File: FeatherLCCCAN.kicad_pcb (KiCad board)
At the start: 2 copper layers, 96.5 x 22.9 mm, 6 parts, among them J301 RJ45, J302 RJ45, U301 TCAN332DR

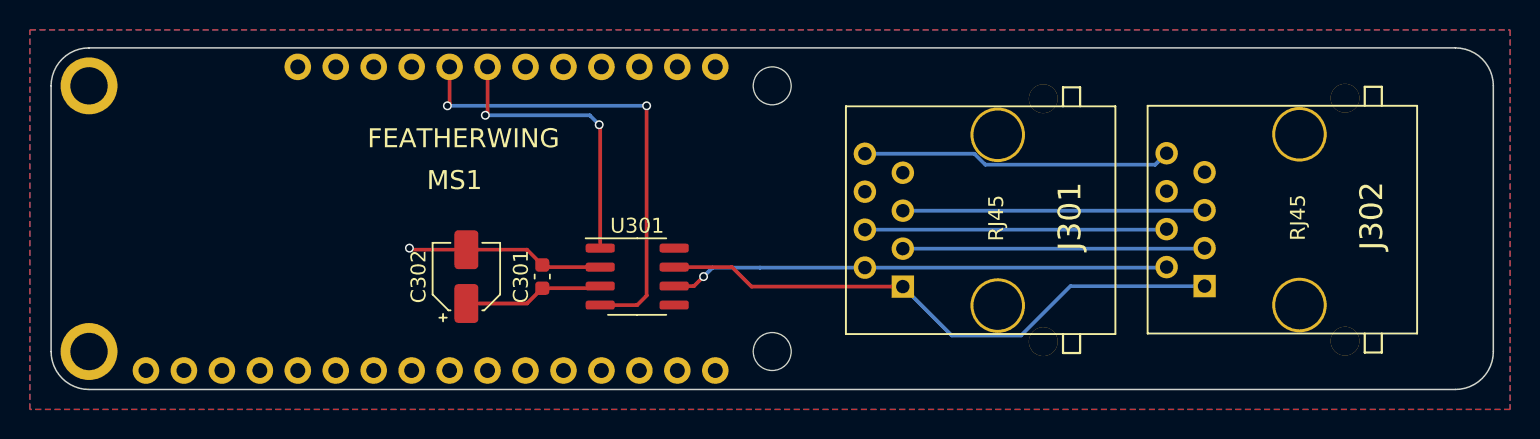
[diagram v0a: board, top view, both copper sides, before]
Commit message: Update part numbers.
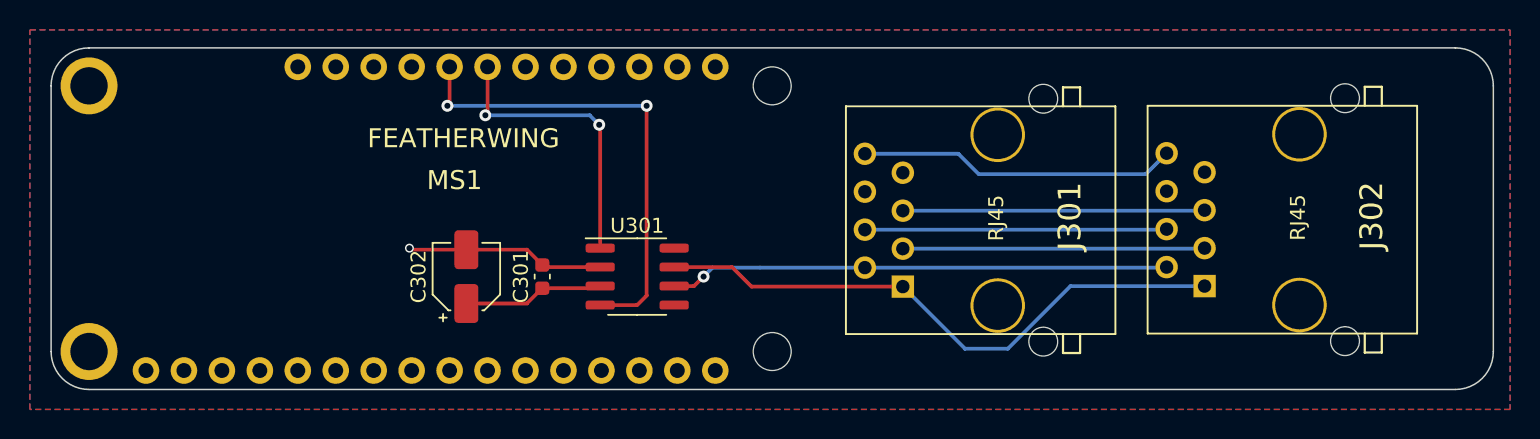
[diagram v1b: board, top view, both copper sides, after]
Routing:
- net /CANH: track 38.8 -> 39.5 mm
- net Net-(J301-Pad8): track 20.8 -> 21.3 mm
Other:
- rule pad_to_mask_clearance: 0.2 -> 0
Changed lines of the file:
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@@
   )
   (setup
-    (pad_to_mask_clearance 0.2)
+    (stackup
+      (layer "F.SilkS" (type "Top Silk Screen"))
+      (layer "F.Paste" (type "Top Solder Paste"))
+      (layer "F.Mask" (type "Top Solder Mask") (thickness 0.01))
+      (layer "F.Cu" (type "copper") (thickness 0.035))
+      (layer "dielectric 1" (type "core") (thickness 1.51) (material "FR4") (epsilon_r 4.5) (loss_tangent 0.02))
+      (layer "B.Cu" (type "copper") (thickness 0.035))
+      (layer "B.Mask" (type "Bottom Solder Mask") (thickness 0.01))
+      (layer "B.Paste" (type "Bottom Solder Paste"))
+      (layer "B.SilkS" (type "Bottom Silk Screen"))
+      (copper_finish "None")
+      (dielectric_constraints no)
+    )
+    (pad_to_mask_clearance 0)
     (pcbplotparams
       (layerselection 0x003ffff_ffffffff)
@@
     (property "Sheetfile" "FeatherLCCCAN.kicad_sch")
     (property "Sheetname" "")
+    (property "exclude_from_bom" "")
+    (attr exclude_from_bom)
     (fp_text reference "J302" (at 0.254 4.826 90) (layer "F.SilkS")
       (effects (font (size 1.524 1.524) (thickness 0.3048)))
@@
     (fp_line (start -8.89 4.3688) (end -7.62 4.3688) (layer "F.SilkS") (width 0.15))
     (fp_line (start 7.62 -10.16) (end -7.62 -10.16) (layer "F.SilkS") (width 0.127))
-    (pad "" thru_hole circle (at -8.128 3.048 90) (size 1.9304 1.9304) (drill 1.9304) (layers *.Cu *.Mask "F.SilkS"))
+    (pad "" np_thru_hole circle (at -8.128 3.048 90) (size 1.9304 1.9304) (drill 1.9304) (layers F&B.Cu *.Mask))
     (pad "" np_thru_hole circle (at 5.715 0 90) (size 3.64998 3.64998) (drill 3.2512) (layers *.Cu *.SilkS *.Mask))
     (pad "" np_thru_hole circle (at -5.715 0 90) (size 3.64998 3.64998) (drill 3.2512) (layers *.Cu *.SilkS *.Mask))
-    (pad "" thru_hole circle (at 8.128 3.048 90) (size 1.9304 1.9304) (drill 1.9304) (layers *.Cu *.Mask "F.SilkS"))
+    (pad "" np_thru_hole circle (at 8.128 3.048 90) (size 1.9304 1.9304) (drill 1.9304) (layers F&B.Cu *.Mask))
     (pad "1" thru_hole rect (at -4.445 -6.35 90) (size 1.50114 1.50114) (drill 0.89916) (layers *.Cu *.Mask "F.SilkS")
       (net 30 "/CANH") (pintype "passive"))
@@
     (descr "SMD capacitor, aluminum electrolytic, United Chemi-Con, 4.0x5.7mm")
     (tags "capacitor electrolytic")
+    (property "LCSC" "C2163057")
+    (property "MPN" "Nichicon UUD1C150MCL1GS")
     (property "Mouser Part Number" "647-UUD1C150MCL")
     (property "Sheetfile" "FeatherLCCCAN.kicad_sch")
@@
     (property "Sheetfile" "FeatherLCCCAN.kicad_sch")
     (property "Sheetname" "")
-    (attr exclude_from_pos_files)
+    (property "exclude_from_bom" "")
+    (attr exclude_from_pos_files exclude_from_bom)
     (fp_text reference "MS1" (at 27 -14) (layer "F.SilkS")
       (effects (font (size 1.27 1.27) (thickness 0.15)))
@@
     (fp_arc (start 93.98 -22.86) (mid 95.776051 -22.116051) (end 96.52 -20.32) (layer "Edge.Cuts") (width 0.1))
     (pad "" np_thru_hole circle (at 48.26 -20.32) (size 2.54 2.54) (drill 2.54) (layers *.Cu *.Mask))
-    (pad "" np_thru_hole circle (at 48.26 -2.54) (size 2.54 2.54) (drill 2.54) (layers *.Cu *.Mask))
+    (pad "" np_thru_hole circle (at 48.26 -2.54) (size 2.54 2.54) (drill 2.54) (layers F&B.Cu))
     (pad "1" thru_hole circle (at 6.35 -1.27) (size 1.778 1.778) (drill 0.99822) (layers *.Cu *.Paste *.Mask)
       (net 13 "/N$18") (pinfunction "~{RESET}") (pintype "input"))
@@
     (descr "Capacitor SMD 0603 (1608 Metric), square (rectangular) end terminal, IPC_7351 nominal, (Body size source: IPC-SM-782 page 76, https://www.pcb-3d.com/wordpress/wp-content/uploads/ipc-sm-782a_amendment_1_and_2.pdf), generated with kicad-footprint-generator")
     (tags "capacitor")
+    (property "LCSC" "C696360")
+    (property "MPN" "KEMET C0603C104M4RAC7411")
     (property "Mouser Part Number" "710-885012206095")
     (property "Sheetfile" "FeatherLCCCAN.kicad_sch")
@@
     (property "Sheetfile" "FeatherLCCCAN.kicad_sch")
     (property "Sheetname" "")
+    (property "exclude_from_bom" "")
+    (attr exclude_from_bom)
     (fp_text reference "J301" (at 0.254 4.826 90) (layer "F.SilkS")
       (effects (font (size 1.524 1.524) (thickness 0.3048)))
@@
     (fp_line (start 8.89 5.5118) (end 8.89 4.3688) (layer "F.SilkS") (width 0.15))
     (pad "" np_thru_hole circle (at -5.715 0 90) (size 3.64998 3.64998) (drill 3.2512) (layers *.Cu *.SilkS *.Mask))
-    (pad "" thru_hole circle (at -8.128 3.048 90) (size 1.9304 1.9304) (drill 1.9304) (layers *.Cu *.Mask "F.SilkS"))
+    (pad "" np_thru_hole circle (at -8.128 3.048 90) (size 1.9304 1.9304) (drill 1.9304) (layers F&B.Cu *.Mask))
     (pad "" np_thru_hole circle (at 5.715 0 90) (size 3.64998 3.64998) (drill 3.2512) (layers *.Cu *.SilkS *.Mask))
-    (pad "" thru_hole circle (at 8.128 3.048 90) (size 1.9304 1.9304) (drill 1.9304) (layers *.Cu *.Mask "F.SilkS"))
+    (pad "" np_thru_hole circle (at 8.128 3.048 90) (size 1.9304 1.9304) (drill 1.9304) (layers F&B.Cu *.Mask))
     (pad "1" thru_hole rect (at -4.445 -6.35 90) (size 1.50114 1.50114) (drill 0.89916) (layers *.Cu *.Mask "F.SilkS")
       (net 30 "/CANH") (pintype "passive"))
@@
     (descr "SOIC, 8 Pin (JEDEC MS-012AA, https://www.analog.com/media/en/package-pcb-resources/package/pkg_pdf/soic_narrow-r/r_8.pdf), generated with kicad-footprint-generator ipc_gullwing_generator.py")
     (tags "SOIC SO")
+    (property "LCSC" "C73651")
+    (property "MPN" "TCAN332DR")
     (property "Mouser Part Number" "595-TCAN332DR")
     (property "Sheetfile" "FeatherLCCCAN.kicad_sch")
@@
   (segment (start 166.37 84.455) (end 165.035 84.455) (width 0.25) (layer "F.Cu") (net 29))
   (segment (start 167.005 83.82) (end 166.37 84.455) (width 0.25) (layer "F.Cu") (net 29))
-  (via (at 167.005 83.82) (size 0.6) (drill 0.4) (layers "F.Cu" "B.Cu") (net 29))
+  (via (at 167.005 83.82) (size 0.8) (drill 0.4) (layers "F.Cu" "B.Cu") (net 29))
   (segment (start 167.6052 83.2198) (end 170.7802 83.2198) (width 0.25) (layer "B.Cu") (net 29))
   (segment (start 167.005 83.82) (end 167.6052 83.2198) (width 0.25) (layer "B.Cu") (net 29))
@@
   (segment (start 170.2148 84.4898) (end 168.91 83.185) (width 0.25) (layer "F.Cu") (net 30))
   (segment (start 168.91 83.185) (end 165.035 83.185) (width 0.25) (layer "F.Cu") (net 30))
+  (segment (start 184.4962 88.646) (end 187.369469 88.646) (width 0.25) (layer "B.Cu") (net 30))
   (segment (start 191.560469 84.455) (end 200.533 84.455) (width 0.25) (layer "B.Cu") (net 30))
-  (segment (start 180.34 84.4898) (end 183.610601 87.760401) (width 0.25) (layer "B.Cu") (net 30))
-  (segment (start 188.255068 87.760401) (end 191.560469 84.455) (width 0.25) (layer "B.Cu") (net 30))
-  (segment (start 183.610601 87.760401) (end 188.255068 87.760401) (width 0.25) (layer "B.Cu") (net 30))
+  (segment (start 187.369469 88.646) (end 191.560469 84.455) (width 0.25) (layer "B.Cu") (net 30))
+  (segment (start 180.34 84.4898) (end 184.4962 88.646) (width 0.25) (layer "B.Cu") (net 30))
   (segment (start 160.085 73.725) (end 160.085 81.915) (width 0.25) (layer "F.Cu") (net 31))
   (segment (start 160.02 73.66) (end 160.085 73.725) (width 0.25) (layer "F.Cu") (net 31))
   (segment (start 152.5484 72.8766) (end 152.5484 69.7848) (width 0.25) (layer "F.Cu") (net 31))
   (segment (start 152.4 73.025) (end 152.5484 72.8766) (width 0.25) (layer "F.Cu") (net 31))
-  (via (at 160.02 73.66) (size 0.6) (drill 0.4) (layers "F.Cu" "B.Cu") (net 31))
-  (via (at 152.4 73.025) (size 0.6) (drill 0.4) (layers "F.Cu" "B.Cu") (net 31))
+  (via (at 160.02 73.66) (size 0.8) (drill 0.4) (layers "F.Cu" "B.Cu") (net 31))
+  (via (at 152.4 73.025) (size 0.8) (drill 0.4) (layers "F.Cu" "B.Cu") (net 31))
   (segment (start 159.385 73.025) (end 152.4 73.025) (width 0.25) (layer "B.Cu") (net 31))
   (segment (start 160.02 73.66) (end 159.385 73.025) (width 0.25) (layer "B.Cu") (net 31))
@@
   (segment (start 163.195 85.09) (end 162.56 85.725) (width 0.25) (layer "F.Cu") (net 32))
   (segment (start 149.86 72.39) (end 150.0084 72.2416) (width 0.25) (layer "F.Cu") (net 32))
-  (via (at 163.195 72.39) (size 0.6) (drill 0.4) (layers "F.Cu" "B.Cu") (net 32))
-  (via (at 149.86 72.39) (size 0.6) (drill 0.4) (layers "F.Cu" "B.Cu") (net 32))
+  (via (at 163.195 72.39) (size 0.8) (drill 0.4) (layers "F.Cu" "B.Cu") (net 32))
+  (via (at 149.86 72.39) (size 0.8) (drill 0.4) (layers "F.Cu" "B.Cu") (net 32))
   (segment (start 149.86 72.39) (end 163.195 72.39) (width 0.25) (layer "B.Cu") (net 32))
-  (segment (start 185.861323 76.330401) (end 197.227599 76.330401) (width 0.25) (layer "B.Cu") (net 35))
-  (segment (start 185.130722 75.5998) (end 185.861323 76.330401) (width 0.25) (layer "B.Cu") (net 35))
-  (segment (start 197.227599 76.330401) (end 197.993 75.565) (width 0.25) (layer "B.Cu") (net 35))
-  (segment (start 177.8 75.5998) (end 185.130722 75.5998) (width 0.25) (layer "B.Cu") (net 35))
+  (segment (start 177.8 75.5998) (end 184.0578 75.5998) (width 0.25) (layer "B.Cu") (net 35))
+  (segment (start 196.596 76.962) (end 197.993 75.565) (width 0.25) (layer "B.Cu") (net 35))
+  (segment (start 185.42 76.962) (end 196.596 76.962) (width 0.25) (layer "B.Cu") (net 35))
+  (segment (start 184.0578 75.5998) (end 185.42 76.962) (width 0.25) (layer "B.Cu") (net 35))
   (zone (net 3) (net_name "+3V3") (layer "F.Cu") (hatch edge 0.508)
     (connect_pads (clearance 0.508))
